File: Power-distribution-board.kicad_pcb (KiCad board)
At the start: 4 copper layers, 101.6 x 113.3 mm, 79 parts, among them J1 178.6165.0001 breaker, J10 2606-1104/020-000, J12 2606-1104/020-000, J13 2606-1104/020-000, J15 2606-1104/020-000, J16 2606-1104/020-000, J2 178.6165.0001 breaker, J3 178.6165.0001 breaker, J4 178.6165.0001 breaker, J5 178.6165.0001 breaker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

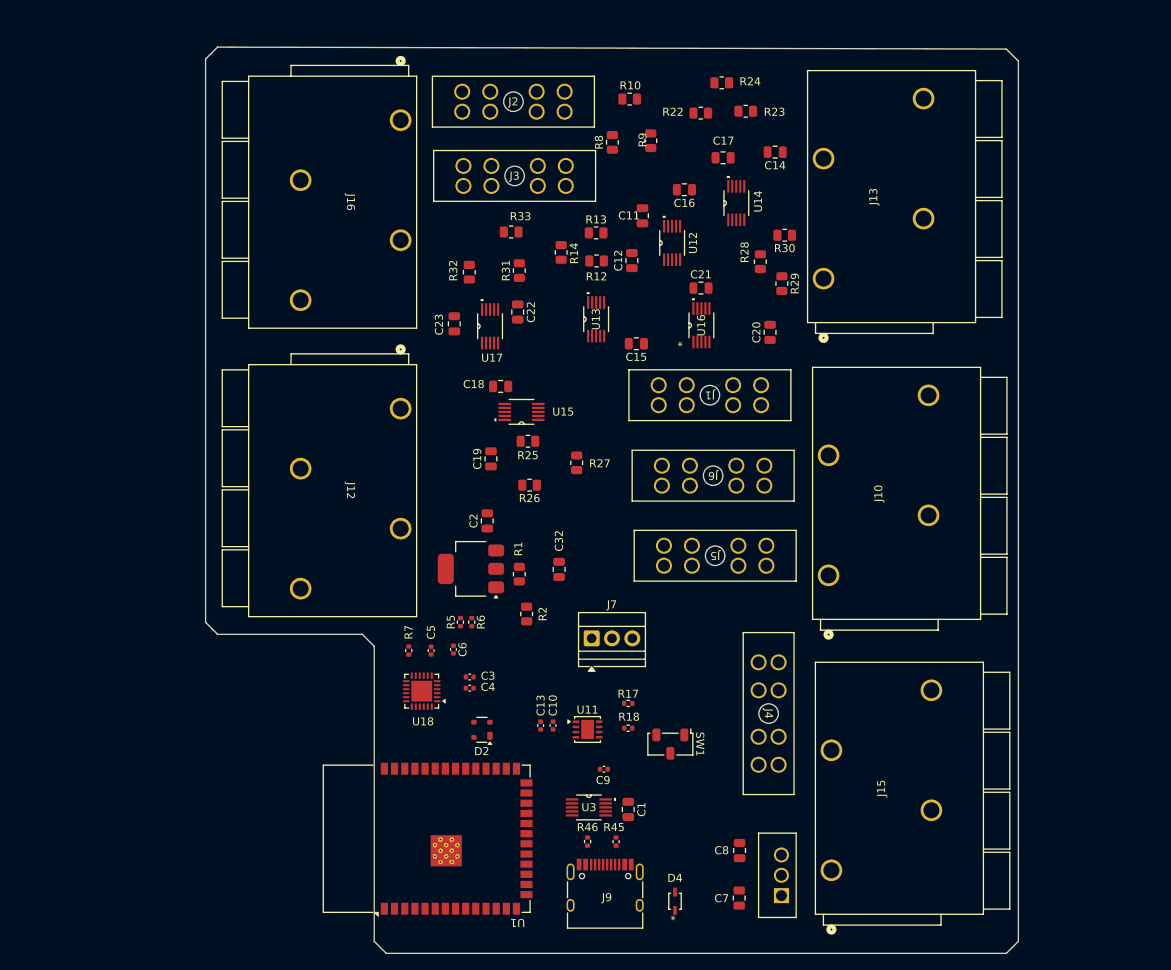
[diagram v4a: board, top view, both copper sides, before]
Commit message: added 4-digit display & pwr planes
add 4digit led and tm1637 driver
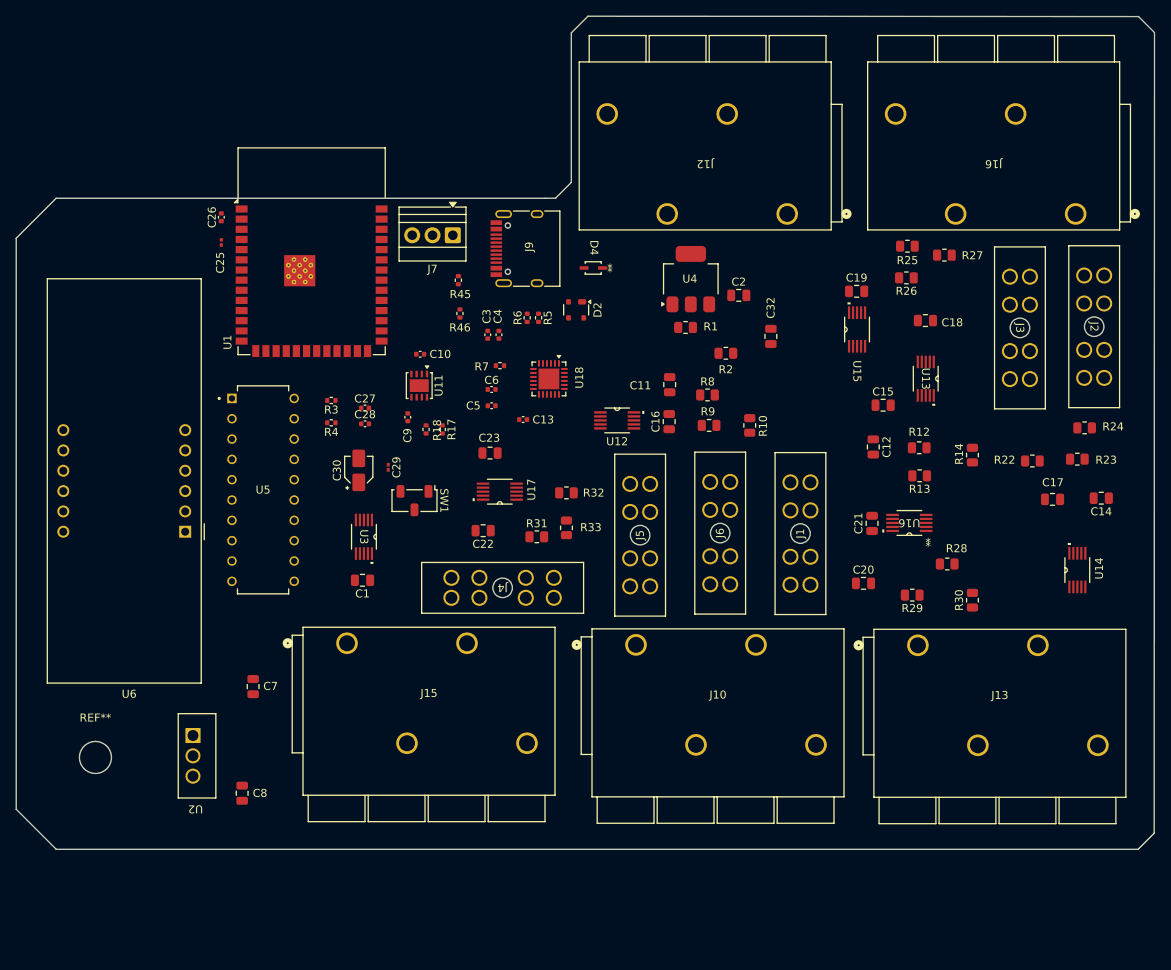
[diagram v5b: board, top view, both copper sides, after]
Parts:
- added C25: 0.1u, Capacitor_SMD:C_0201_0603Metric, F.Cu at (90.9, 63.8)
- added C26: 10u, Capacitor_SMD:C_0402_1005Metric, F.Cu at (90.9, 60.6)
- added C27: 100p, Capacitor_SMD:C_0402_1005Metric, F.Cu at (108.8, 84.5)
- added C28: 100p, Capacitor_SMD:C_0402_1005Metric, F.Cu at (108.8, 86.5)
- added C29: 0.1u, Capacitor_SMD:C_0201_0603Metric, F.Cu at (111.7, 91.9)
- added C30: 100u, Capacitor_SMD:CP_Elec_3x5.4, F.Cu at (108.0, 92.3)
- added R3: 10k, Resistor_SMD:R_0402_1005Metric, F.Cu at (104.6, 83.5)
- added R4: 10k, Resistor_SMD:R_0402_1005Metric, F.Cu at (104.6, 86.3)
- added REF**: MountingHole_4mm, MountingHole:MountingHole_4mm, F.Cu at (75.1, 128.2)
- added U5: TM1637, pdb_footprints:LED_driver_TM1637, F.Cu at (96.1, 94.7)
- added U6: CC56-12EWA, Display_7Segment:CA56-12EWA, F.Cu at (86.4, 100.0)
- moved J16 85.2 mm to (197.7, 60.2), turned to 180 degrees
- moved J9 81.6 mm to (129.3, 64.6), turned to 90 degrees
- moved D4 79.8 mm to (137.4, 67.0), turned to 180 degrees
- moved U1 74.8 mm to (102.2, 64.9), turned to 0 degrees
- moved J2 73.0 mm to (198.7, 80.7), turned to -90 degrees
- moved R45 72.9 mm to (120.5, 68.5), turned to -90 degrees
- moved U2 72.2 mm to (88.3, 130.5), turned to -90 degrees
- moved R46 67.9 mm to (120.7, 72.7), turned to -90 degrees
- moved J15 66.9 mm to (106.6, 113.9), turned to 0 degrees
- moved C7 66.3 mm to (94.8, 119.3), turned to -90 degrees
- moved U14 62.6 mm to (197.9, 104.7)
- moved R24 62.6 mm to (198.8, 87.0)
- moved C8 62.6 mm to (93.5, 132.6), turned to 90 degrees
- moved J3 60.5 mm to (189.4, 80.9), turned to -90 degrees
- moved R22 60.1 mm to (192.3, 91.1)
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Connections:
- U1 pad 31: unconnected-(U1-IO38-Pad31) -> /CLK
- U1 pad 32: unconnected-(U1-IO39-Pad32) -> /DIO
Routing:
- added copper zone on In2.Cu, net /3.3V
- added copper zone on In2.Cu, net /5V
- added copper zone on In2.Cu, net /BAT+
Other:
- board size 101.6 x 113.3 mm -> 142.3 x 104.1 mm

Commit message: added 15vin pwr plane cus i forgot
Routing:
- added copper zone on In2.Cu, net /15VIN
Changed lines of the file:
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@@
 		(tags "CMS SOT")
 		(property "Reference" "U4"
-			(at 0.0286 -0.122601 -180)
+			(at 0.0286 -0.122601 180)
 			(layer "F.SilkS")
 			(effects
@@
 			)
 		)
+	)
+	(zone
+		(net 4)
+		(net_name "/15VIN")
+		(layer "In2.Cu")
+		(hatch edge 0.5)
+		(priority 5)
+		(connect_pads
+			(clearance 0.5)
+		)
+		(min_thickness 0.25)
+		(filled_areas_thickness no)
+		(fill yes
+			(thermal_gap 0.5)
+			(thermal_bridge_width 0.5)
+		)
+		(polygon
+			(pts
+				(xy 195.4784 65.0748) (xy 185.6232 65.1764) (xy 185.8772 56.4388) (xy 157.0736 56.5404) (xy 155.2956 72.4408)
+				(xy 150.622 72.7964) (xy 150.9268 70.4596) (xy 152.5016 69.7992) (xy 153.416 50.3936) (xy 194.8688 50.4952)
+				(xy 195.4784 65.0748)
+			)
+		)
